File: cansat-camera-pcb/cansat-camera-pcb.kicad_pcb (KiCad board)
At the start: 2 copper layers, 68 parts, among them IC2 TLV74315PDBVR, J1 Conn_01x08_Pin, J2 Micro_SD_Card_Det2, J4 Conn_02x10_Odd_Even, J5 Conn_02x10_Odd_Even, J6 OV5640, SW2 SW_Push, U1 IS42S16800F-5TLI, U2 AP2112K-3.3, U4 STM32H743ZITx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

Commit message: Update cansat-camera-pcb.kicad_pcb
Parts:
- C1, C25, C26, C27, C28, C29, C30, C31, C32, C33, C34, J6, U1, Y1: moved to B.Cu
- moved Y1 196.2 mm to (230.8, 51.3), turned to -90 degrees
- moved C2 185.1 mm to (231.4, 57.9), turned to 180 degrees
- moved C1 184.9 mm to (230.6, 58.8)
- moved C4 181.8 mm to (230.2, 47.8), turned to -90 degrees
- moved U4 181.2 mm to (215.9, 54.0), turned to 180 degrees
- moved SW2 180.2 mm to (231.4, 54.3), turned to -90 degrees
- moved C3 179.8 mm to (228.0, 47.8), turned to 90 degrees
- moved C34 178.7 mm to (230.5, 43.8), turned to 180 degrees
- moved R1 176.7 mm to (229.8, 49.2)
- moved R2 175.5 mm to (229.1, 47.8), turned to 90 degrees
- moved R14 171.8 mm to (222.1, 66.2), turned to 180 degrees
- moved C9 166.7 mm to (212.9, 66.2)
- moved C12 165.6 mm to (217.4, 41.9), turned to 180 degrees
- moved C35 158.6 mm to (208.6, 41.7)
- moved C10 156.5 mm to (203.8, 62.9), turned to -90 degrees
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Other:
- board outline added: 50 x 50 mm

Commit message: Alkatrész elhelyezés final
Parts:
- removed C37: 100nF, Capacitor_SMD:C_0402_1005Metric
- removed C39, C45, C46, C7: 10uF, Capacitor_SMD:C_0603_1608Metric
- C1, C34: moved to F.Cu
- C38, C5, C6: value 10uF -> 1uF; moved to B.Cu
- C40, C41, C42, C43, C44, IC2, JP1, R16, R17, R4, R5, TP1, U6: moved to B.Cu
- J1: footprint Connector_PinSocket_2.54mm:PinSocket_1x08_P2.54mm_Vertical -> Connector_PinHeader_2.54mm:PinHeader_1x08_P2.54mm_Vertical_SMD_Pin1Left; moved to B.Cu
- J4, J5: footprint Connector_PinSocket_2.00mm:PinSocket_2x10_P2.00mm_Vertical -> Connector_PinHeader_2.00mm:PinHeader_2x10_P2.00mm_Vertical_SMD
- R11: value 10k -> 47k
- Y1: footprint Crystal:Crystal_SMD_HC49-SD -> Crystal:Crystal_SMD_3225-4Pin_3.2x2.5mm; moved to F.Cu
- moved C2 184.6 mm to (55.9, 115.2)
- moved SW2 184.6 mm to (55.9, 111.7)
- moved C34 158.7 mm to (86.8, 111.2)
- moved Y1 156.6 mm to (87.2, 113.8)
- moved C4 155.7 mm to (87.4, 109.8)
- moved R2 155.5 mm to (86.5, 109.8)
- moved C10 155.3 mm to (61.4, 124.9)
- moved C11 155.3 mm to (61.4, 118.1)
- moved C13 155.3 mm to (60.2, 112.6)
- moved C8 155.3 mm to (61.4, 112.6)
- moved C12 155.3 mm to (75.0, 104.0)
- moved C3 155.3 mm to (85.6, 109.8)
- moved C35 155.3 mm to (66.2, 103.7)
- moved C36 155.3 mm to (61.1, 122.6)
- moved C9 155.3 mm to (70.5, 128.2)
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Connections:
- J4 pad 1: /I2C4_SDA -> /I2C2_SDA
- J4 pad 11: /USART2_TX -> unconnected-(J4-Pin_11-Pad11)
- J4 pad 13: /USART2_RX -> unconnected-(J4-Pin_13-Pad13)
- J4 pad 14: unconnected-(J4-Pin_14-Pad14) -> /USART2_TX
- J4 pad 16: unconnected-(J4-Pin_16-Pad16) -> /USART2_RX
- J4 pad 2: /I2C2_SDA -> /I2C4_SDA
- J4 pad 3: /I2C4_SCL -> /I2C2_SCL
- J4 pad 4: /I2C2_SCL -> /I2C4_SCL
- J4 pad 6: unconnected-(J4-Pin_6-Pad6) -> GND
- J4 pad 7: GND -> unconnected-(J4-Pin_7-Pad7)
- J4 pad 8: unconnected-(J4-Pin_8-Pad8) -> GND
- J4 pad 9: GND -> unconnected-(J4-Pin_9-Pad9)

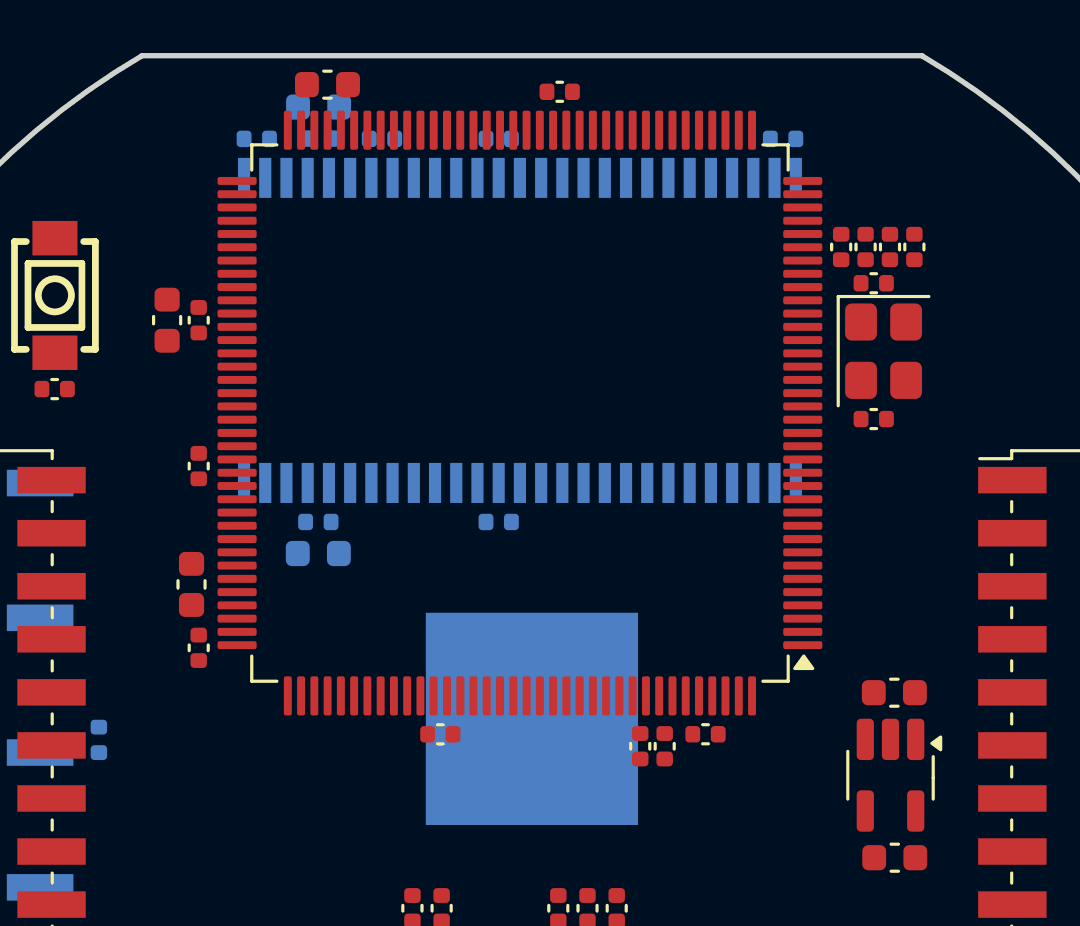
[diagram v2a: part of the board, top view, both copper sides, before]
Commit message: Sdram finish, stm részben
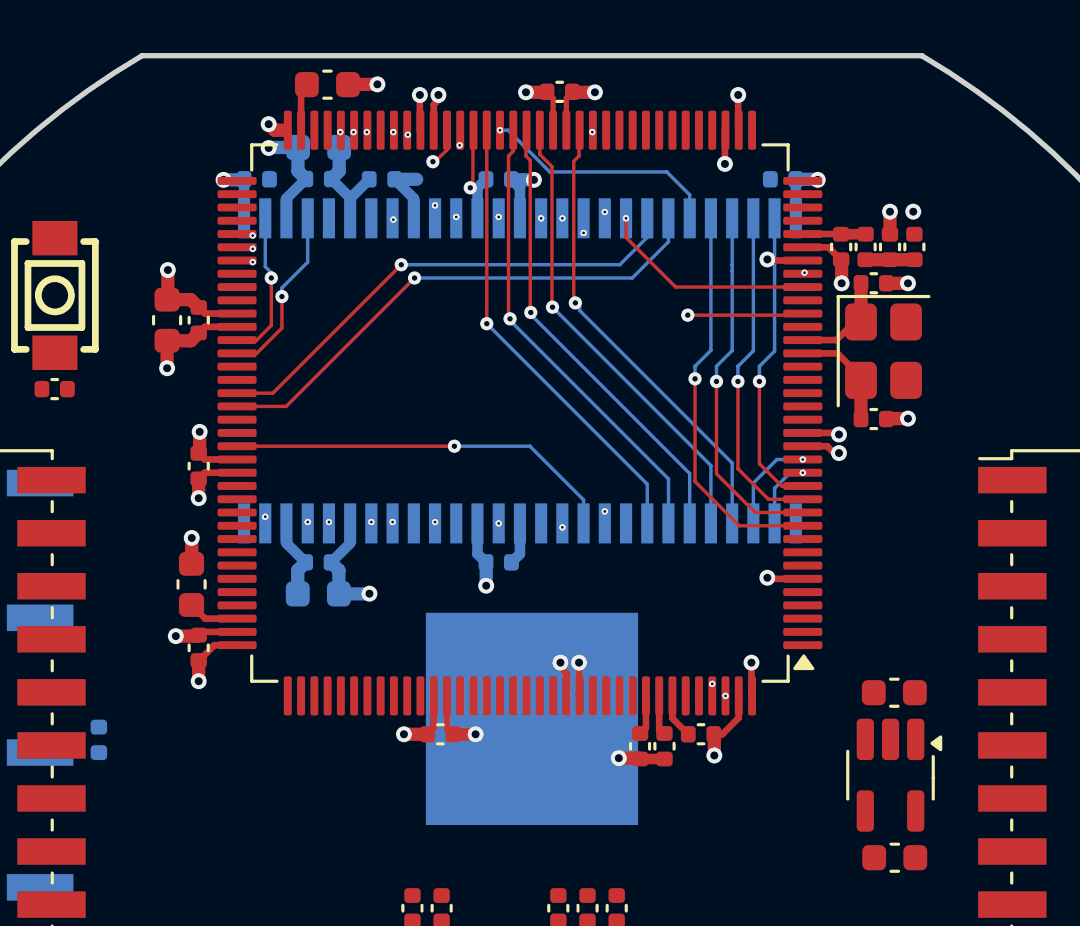
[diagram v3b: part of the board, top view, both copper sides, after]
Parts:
- moved C25 1.52 mm to (65.9, 107.3)
- moved C26 1.52 mm to (68.3, 107.3)
- moved C27 1.52 mm to (72.7, 107.3)
- moved C28 1.52 mm to (65.9, 122.9)
- moved C29 1.52 mm to (83.4, 107.3)
- moved C30 1.52 mm to (65.9, 121.7)
- moved C31 1.52 mm to (72.7, 121.7)
- moved C32 1.52 mm to (63.6, 107.3)
- moved C33 1.52 mm to (65.9, 106.1), turned to 0 degrees
- moved U1 1.52 mm to (73.5, 114.5)
- moved R14 0.17 mm to (80.3, 128.2)
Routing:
- net +3.3V: track 0.00 -> 45.7 mm, vias 0 -> 22
- net GND: track 0.00 -> 40.3 mm, vias 0 -> 16
- net /FMC_NBL0: track 0.00 -> 20.2 mm, vias 0 -> 2
- net /FMC_BA1: track 0.00 -> 19.7 mm, vias 0 -> 1
- net /FMC_BA0: track 0.00 -> 18.6 mm, vias 0 -> 1
- net /FMC_SDNCAS: track 0.00 -> 17.6 mm, vias 0 -> 2
- net /FMC_A9: track 0.00 -> 17.5 mm, vias 0 -> 1
- net /FMC_A7: track 0.00 -> 17.5 mm, vias 0 -> 1
- net /FMC_A6: track 0.00 -> 17.4 mm, vias 0 -> 1
- net /FMC_A8: track 0.00 -> 17.4 mm, vias 0 -> 1
- net /FMC_A11: track 0.00 -> 17.3 mm, vias 0 -> 1
- net /FMC_D8: track 0.00 -> 16.9 mm, vias 0 -> 2
- net /FMC_D10: track 0.00 -> 15.8 mm, vias 0 -> 2
- net /FMC_D11: track 0.00 -> 15.3 mm, vias 0 -> 2
- net /FMC_D12: track 0.00 -> 15.2 mm, vias 0 -> 2
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- added copper zone on In4.Cu, net +3.3V
- added copper zone on In1.Cu, net GND
- added copper zone on In3.Cu, net GND
- added copper zone on In6.Cu, net GND
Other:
- copper layers 2 -> 8

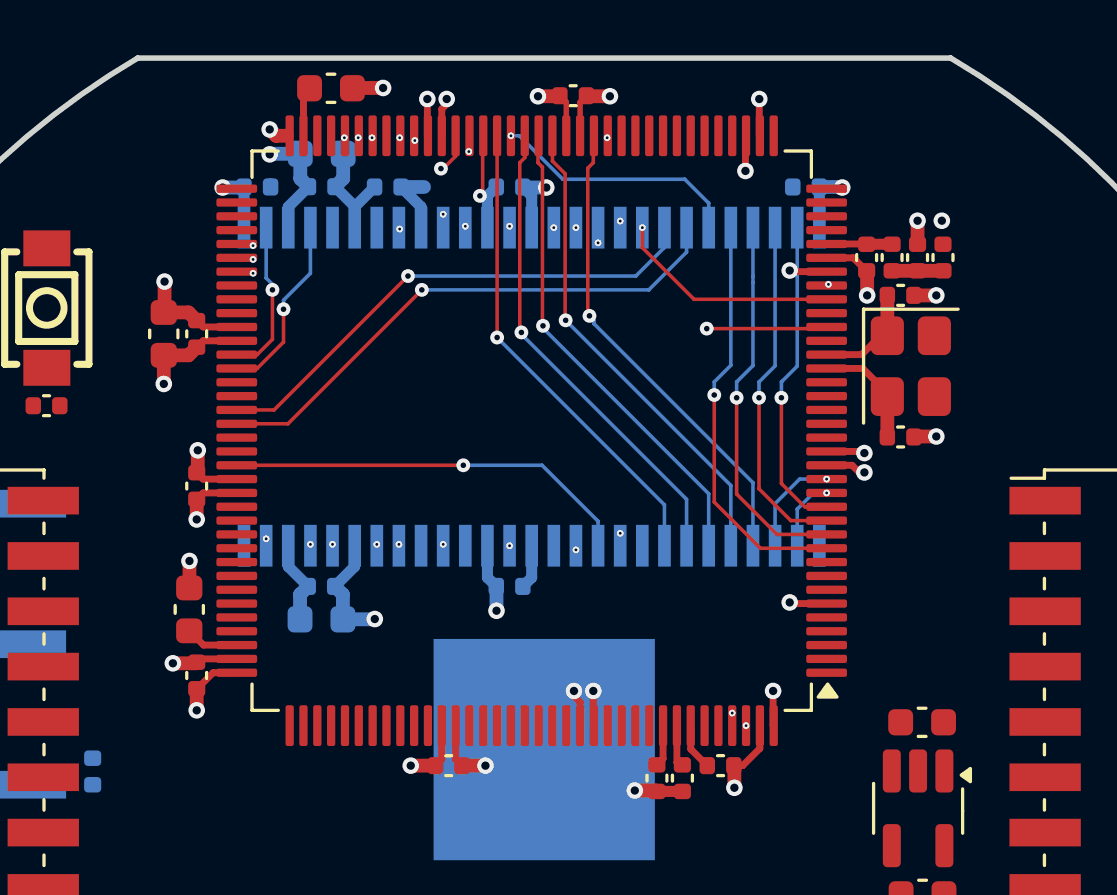
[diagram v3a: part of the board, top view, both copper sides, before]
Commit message: Routing tisztázás (sdram, stm)
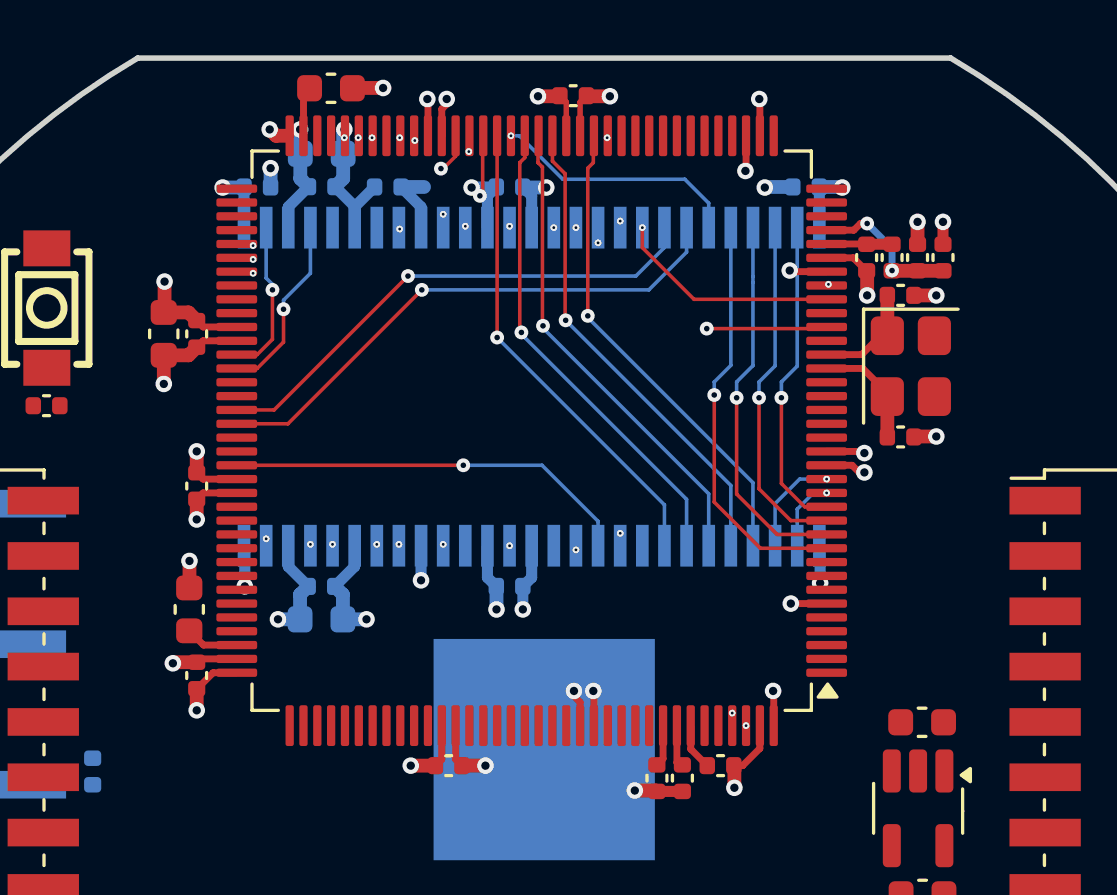
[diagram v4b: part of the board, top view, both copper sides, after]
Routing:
- net GND: track 40.3 -> 49.4 mm, vias 16 -> 25
- net /VDDA_PIN: track 1.84 -> 5.48 mm, vias 0 -> 2

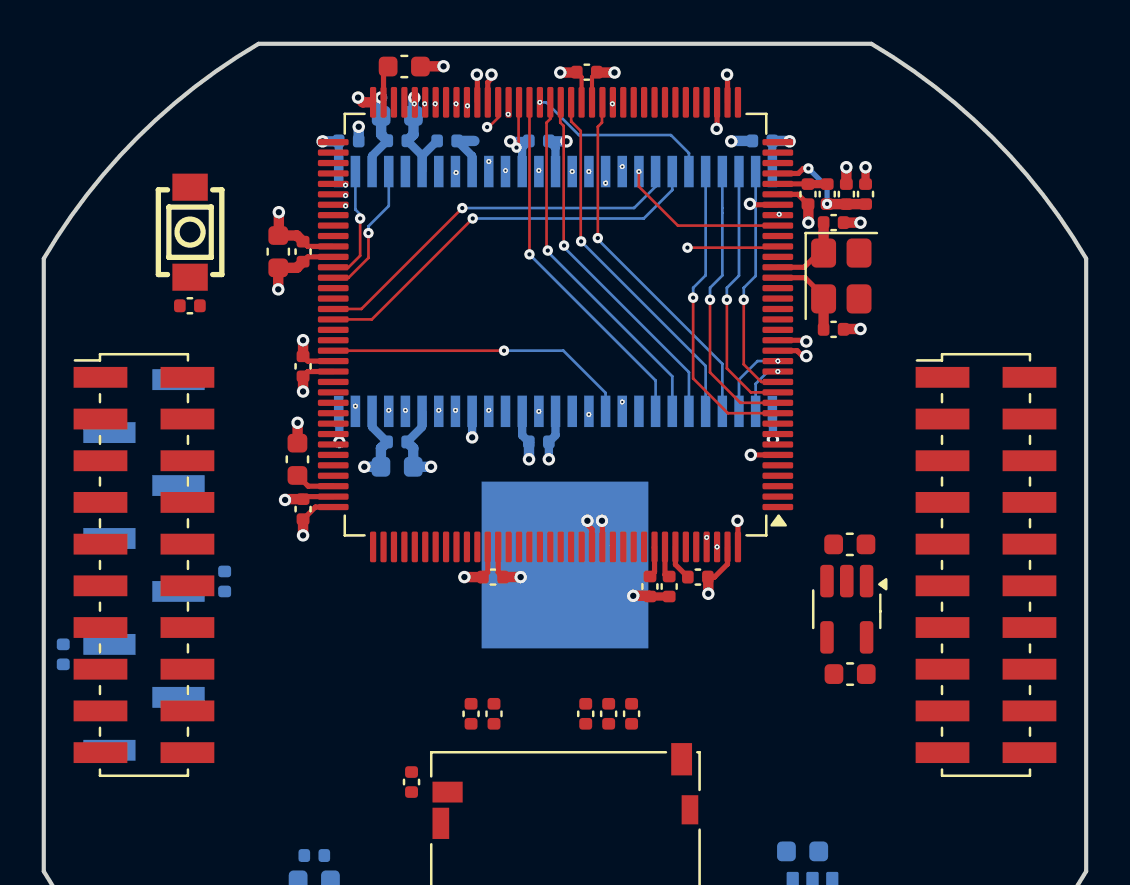
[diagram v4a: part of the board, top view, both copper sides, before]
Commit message: Stm32, Sdram routolás végleges
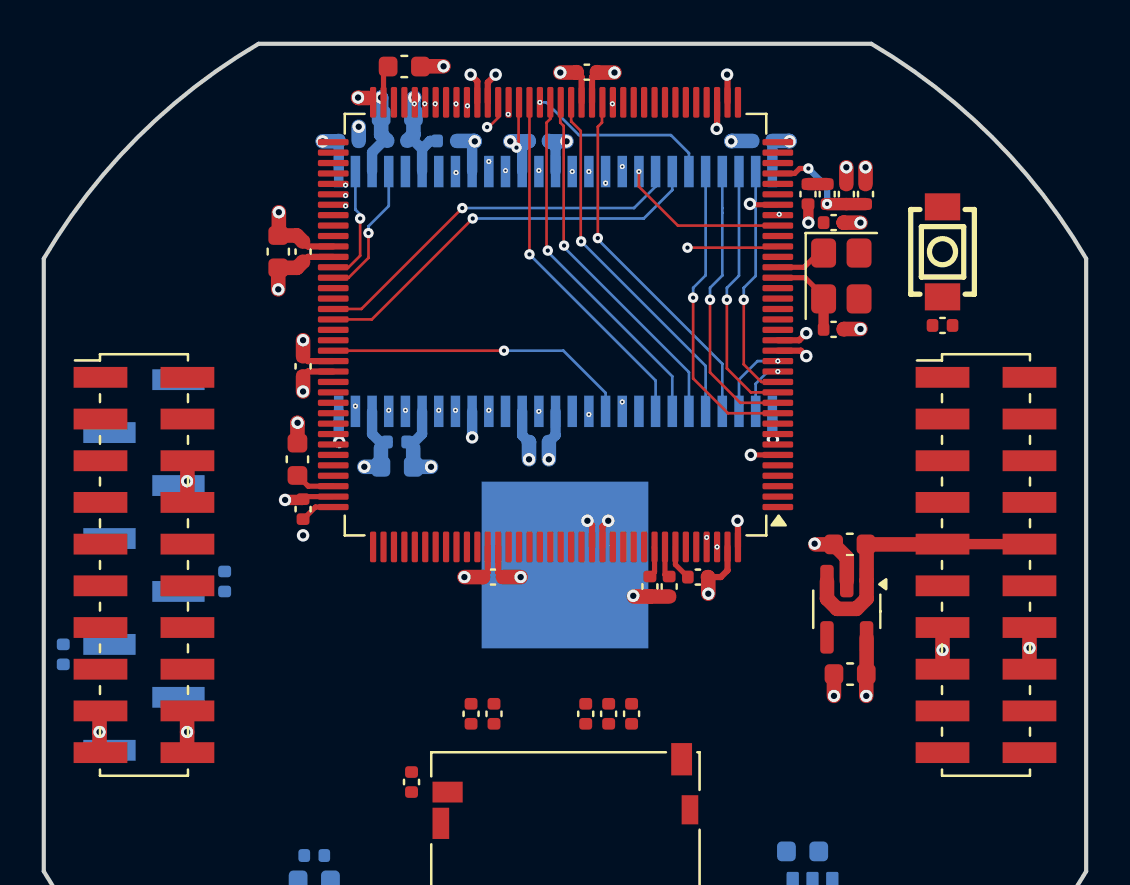
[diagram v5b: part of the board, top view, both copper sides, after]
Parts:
- moved C2 36.1 mm to (92.0, 116.1)
- moved SW2 36.1 mm to (92.0, 112.6)
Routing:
- net VCC: track 0.00 -> 14.4 mm
- net GND: track 49.4 -> 61.3 mm, vias 25 -> 32
- net +3.3V: track 45.9 -> 47.9 mm, vias 22 -> 23
- net Net-(U4-PH1): track 3.94 -> 2.48 mm
- net /VREF_PIN: track 2.37 -> 0.92 mm

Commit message: Routolás folytatása
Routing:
- net GND: track 61.3 -> 63.5 mm, vias 32 -> 34
- net /RST: track 0.00 -> 1.57 mm
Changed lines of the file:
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@@
+	)
+	(segment
+		(start 90.6 116.13)
+		(end 91.555 116.13)
+		(width 0.7)
+		(layer "F.Cu")
+		(net 1)
 	)
 	(segment
@@
 	)
 	(segment
+		(start 92.035 109.2)
+		(end 92.035 110.441)
+		(width 0.7)
+		(layer "F.Cu")
+		(net 1)
+	)
+	(segment
 		(start 61.092012 121.776)
 		(end 61.092012 120.807988)
@@
 	)
 	(via blind
+		(at 90.6 116.13)
+		(size 0.6)
+		(drill 0.3)
+		(layers "F.Cu" "In1.Cu")
+		(free yes)
+		(net 1)
+	)
+	(via blind
 		(at 60.2 110.7)
 		(size 0.6)
@@
 	(via blind
 		(at 86.827 133.9)
+		(size 0.6)
+		(drill 0.3)
+		(layers "F.Cu" "In1.Cu")
+		(free yes)
+		(net 1)
+	)
+	(via blind
+		(at 92.035 109.2)
 		(size 0.6)
 		(drill 0.3)
@@
 		(layer "F.Cu")
 		(net 2)
+	)
+	(segment
+		(start 92.515 116.13)
+		(end 92.515 115.239)
+		(width 0.3)
+		(layer "F.Cu")
+		(net 3)
+	)
+	(segment
+		(start 92.515 115.239)
+		(end 92.035 114.759)
+		(width 0.3)
+		(layer "F.Cu")
+		(net 3)
 	)
 	(segment
@@
 	)
 	(segment
+		(start 86.492 129.236544)
+		(end 86.492 128.393)
+		(width 0.7)
+		(layer "F.Cu")
+		(net 7)
+	)
+	(segment
+		(start 88.362 126.633)
+		(end 92.022 126.633)
+		(width 0.7)
+		(layer "F.Cu")
+		(net 7)
+	)
+	(segment
+		(start 87.904544 129.724)
+		(end 86.979456 129.724)
+		(width 0.7)
+		(layer "F.Cu")
+		(net 7)
+	)
+	(segment
+		(start 86.492 128.393)
+		(end 86.492 129.095122)
+		(width 0.5)
+		(layer "F.Cu")
+		(net 7)
+	)
+	(segment
 		(start 96.205 126.62)
 		(end 92.035 126.62)
-		(width 0.5)
+		(width 0.7)
 		(layer "F.Cu")
 		(net 7)
-	)
-	(segment
-		(start 86.492 129.236544)
-		(end 86.492 128.393)
-		(width 0.7)
-		(layer "F.Cu")
-		(net 7)
-	)
-	(segment
-		(start 88.362 126.633)
-		(end 92.022 126.633)
-		(width 0.7)
-		(layer "F.Cu")
-		(net 7)
-	)
-	(segment
-		(start 87.904544 129.724)
-		(end 86.979456 129.724)
-		(width 0.7)
-		(layer "F.Cu")
-		(net 7)
-	)
-	(segment
-		(start 86.492 128.393)
-		(end 86.492 129.095122)
-		(width 0.5)
-		(layer "F.Cu")
-		(net 7)

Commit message: Routolás folytatása
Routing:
- net GND: track 63.5 -> 87.7 mm, vias 34 -> 45
- net +3.3V: track 47.9 -> 71.9 mm, vias 23 -> 32
- net /camera/DATA1: track 0.00 -> 7.37 mm
- net /camera/2.8V_camera: track 0.00 -> 2.92 mm
- net /camera/1.5V_camera: track 0.00 -> 2.91 mm
- net /OV5640_RESET: track 0.00 -> 2.22 mm
- net /DCMI_PIXCLK: track 0.00 -> 1.38 mm
